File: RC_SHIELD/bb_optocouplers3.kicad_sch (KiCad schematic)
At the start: 15 parts, among them J1 Conn_01x04, U1 SFH6345, U2 SFH6345

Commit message: added secondary MCU to schematic and made it more consistent
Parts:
- removed J1 (x3): Conn_01x04, Connector_RJ:RJ9_Evercom_5301-440xxx_Horizontal, symbol Connector_Generic:Conn_01x04
- added R1 (x3), R2 (x3): 1K2, symbol Device:R
- added U1 (x3), U2 (x3): SFH6345, SFH6345:DIP762W50P254L977H451Q8, symbol SFH6345:SFH6345
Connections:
- net +3V3: now also U1.8, U1.8, U1.8, U2.8, U2.8, U2.8
- net GND: now also U2.5, U2.5, U2.5
- net GNDPWR: now also R1.2, R1.2, R1.2, R2.2, R2.2, R2.2
- net PHI_LIM_L_24: now reaches U2.2
- net PHI_LIM_R_24: now reaches U1.2
- net Z_LIM_TOP_24: now reaches U1.2
- net Z_LIM_BOT_24: now reaches U2.2
- net R_LIM_IN_24: now reaches U1.2
- net R_LIM_OUT_24: now reaches U2.2
- new net: R1.1, U1.3 (x3)
- new net: R2.1, U2.3 (x3)
- new net ALF_LIM_L: U2.6
- new net ALF_LIM_L_24: U2.2
- new net ALF_LIM_R: U1.6
- new net ALF_LIM_R_24: U1.2
- new net BET_LIM_DOWN: U2.6
- new net BET_LIM_DOWN_24: U2.2
- new net BET_LIM_UP: U1.6
- new net BET_LIM_UP_24: U1.2
- new net TH_LIM_CCW: U1.6
- new net TH_LIM_CCW_24: U1.2
- new net TH_LIM_CLW: U2.6
- new net TH_LIM_CLW_24: U2.2
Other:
- note removed: "PHI LimSwitch"
- note removed: "R LimSwitch"
- note removed: "Z LimSwitch"
- company: (none) -> LEGO Kör (legokor.hu)
- title: LIMIT SWITCHES -> Karcsi (INDACT Robot Arm) - limit switch optocouplers
- moved on the sheet: R1, R2, U1, U2

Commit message: footprints assigned
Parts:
- R1, R2: footprint (none) -> Resistor_SMD:R_0805_2012Metric_Pad1.20x1.40mm_HandSolder
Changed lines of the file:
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@@
       (effects (font (size 1.27 1.27)) (justify left))
     )
-    (property "Footprint" "" (at 211.582 45.085 90)
+    (property "Footprint" "Resistor_SMD:R_0805_2012Metric_Pad1.20x1.40mm_HandSolder" (at 211.582 45.085 90)
       (effects (font (size 1.27 1.27)) hide)
     )
@@
       (effects (font (size 1.27 1.27)) (justify left))
     )
-    (property "Footprint" "" (at 212.217 173.355 90)
+    (property "Footprint" "Resistor_SMD:R_0805_2012Metric_Pad1.20x1.40mm_HandSolder" (at 212.217 173.355 90)
       (effects (font (size 1.27 1.27)) hide)
     )
@@
       (effects (font (size 1.27 1.27)) (justify left))
     )
-    (property "Footprint" "" (at 111.887 86.995 90)
+    (property "Footprint" "Resistor_SMD:R_0805_2012Metric_Pad1.20x1.40mm_HandSolder" (at 111.887 86.995 90)
       (effects (font (size 1.27 1.27)) hide)
     )
@@
       (effects (font (size 1.27 1.27)) (justify left))
     )
-    (property "Footprint" "" (at 35.052 45.085 90)
+    (property "Footprint" "Resistor_SMD:R_0805_2012Metric_Pad1.20x1.40mm_HandSolder" (at 35.052 45.085 90)
       (effects (font (size 1.27 1.27)) hide)
     )
@@
       (effects (font (size 1.27 1.27)) (justify left))
     )
-    (property "Footprint" "" (at 35.052 86.995 90)
+    (property "Footprint" "Resistor_SMD:R_0805_2012Metric_Pad1.20x1.40mm_HandSolder" (at 35.052 86.995 90)
       (effects (font (size 1.27 1.27)) hide)
     )
@@
       (effects (font (size 1.27 1.27)) (justify left))
     )
-    (property "Footprint" "" (at 111.887 131.445 90)
+    (property "Footprint" "Resistor_SMD:R_0805_2012Metric_Pad1.20x1.40mm_HandSolder" (at 111.887 131.445 90)
       (effects (font (size 1.27 1.27)) hide)
     )
@@
       (effects (font (size 1.27 1.27)) (justify left))
     )
-    (property "Footprint" "" (at 35.052 173.355 90)
+    (property "Footprint" "Resistor_SMD:R_0805_2012Metric_Pad1.20x1.40mm_HandSolder" (at 35.052 173.355 90)
       (effects (font (size 1.27 1.27)) hide)
     )
@@
       (effects (font (size 1.27 1.27)) (justify left))
     )
-    (property "Footprint" "" (at 212.217 131.445 90)
+    (property "Footprint" "Resistor_SMD:R_0805_2012Metric_Pad1.20x1.40mm_HandSolder" (at 212.217 131.445 90)
       (effects (font (size 1.27 1.27)) hide)
     )
@@
       (effects (font (size 1.27 1.27)) (justify left))
     )
-    (property "Footprint" "" (at 111.887 173.355 90)
+    (property "Footprint" "Resistor_SMD:R_0805_2012Metric_Pad1.20x1.40mm_HandSolder" (at 111.887 173.355 90)
       (effects (font (size 1.27 1.27)) hide)
     )
@@
       (effects (font (size 1.27 1.27)) (justify left))
     )
-    (property "Footprint" "" (at 111.887 45.085 90)
+    (property "Footprint" "Resistor_SMD:R_0805_2012Metric_Pad1.20x1.40mm_HandSolder" (at 111.887 45.085 90)
       (effects (font (size 1.27 1.27)) hide)
     )
@@
       (effects (font (size 1.27 1.27)) (justify left))
     )
-    (property "Footprint" "" (at 35.052 131.445 90)
+    (property "Footprint" "Resistor_SMD:R_0805_2012Metric_Pad1.20x1.40mm_HandSolder" (at 35.052 131.445 90)
       (effects (font (size 1.27 1.27)) hide)
     )
@@
       (effects (font (size 1.27 1.27)) (justify left))
     )
-    (property "Footprint" "" (at 211.582 86.995 90)
-      (effects (font (size 1.27 1.27)) hide)
-    )
+    (property "Footprint" "Resistor_SMD:R_0805_2012Metric_Pad1.20x1.40mm_HandSolder" (at 211.582 86.995 90)
+      (effects (font (size 1.27 1.27)) hide)
+    )

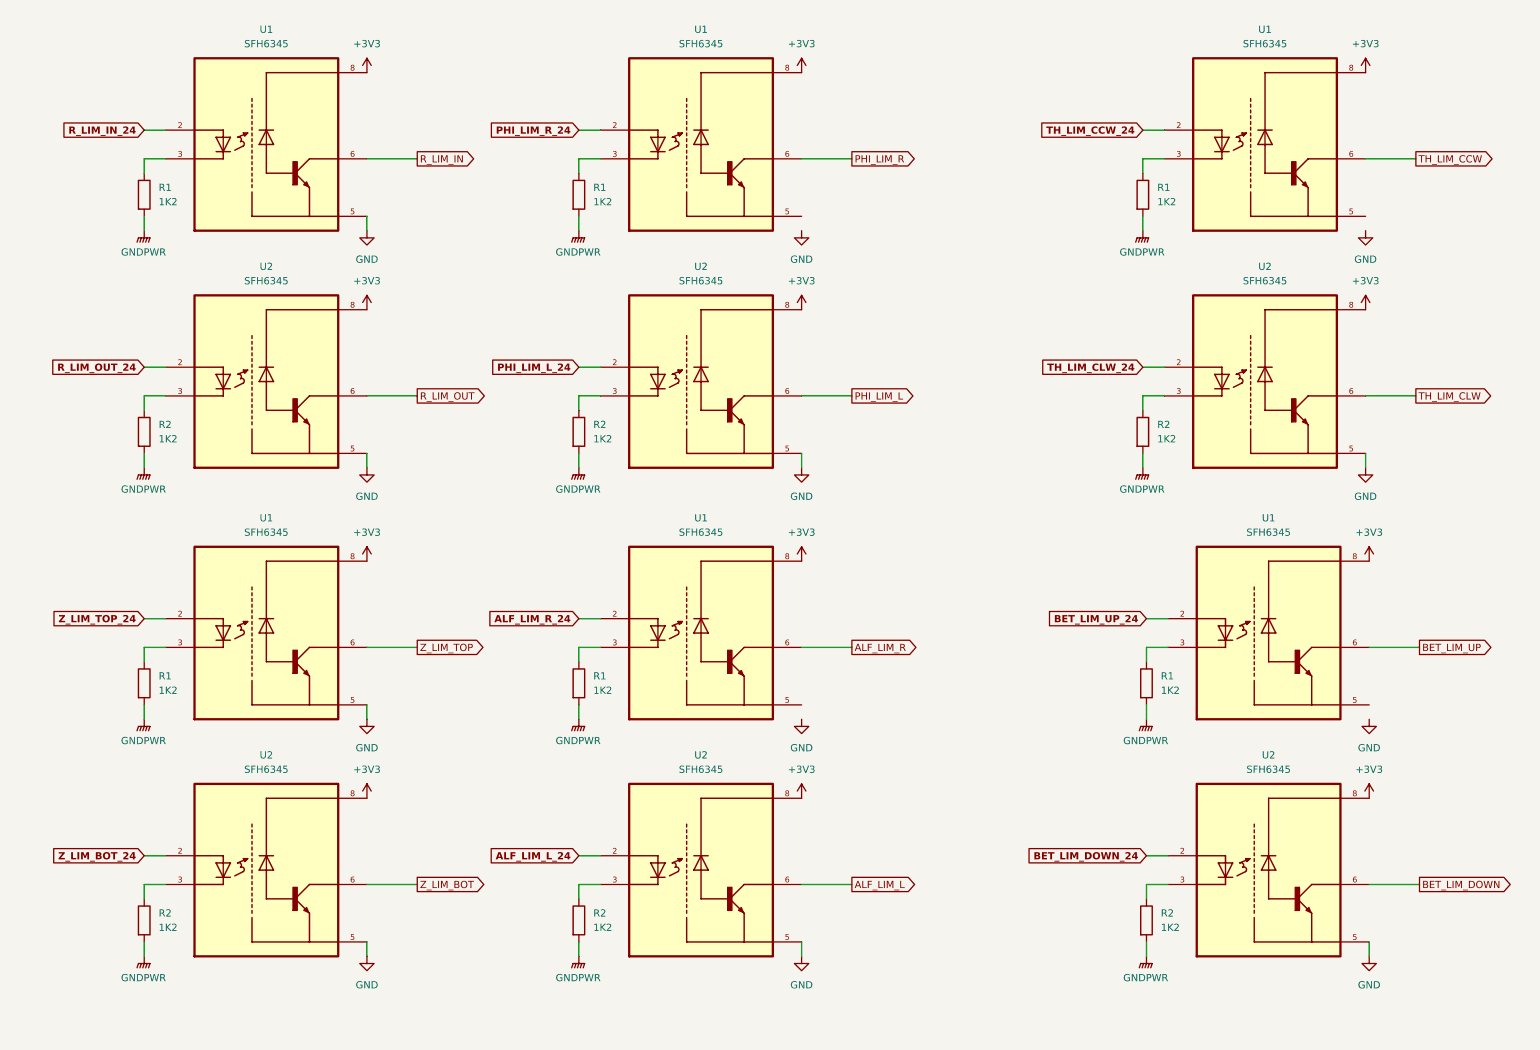
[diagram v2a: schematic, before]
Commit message: Fixed typos and names in schematic, changed optocoupler resistors; added .gitgnore file
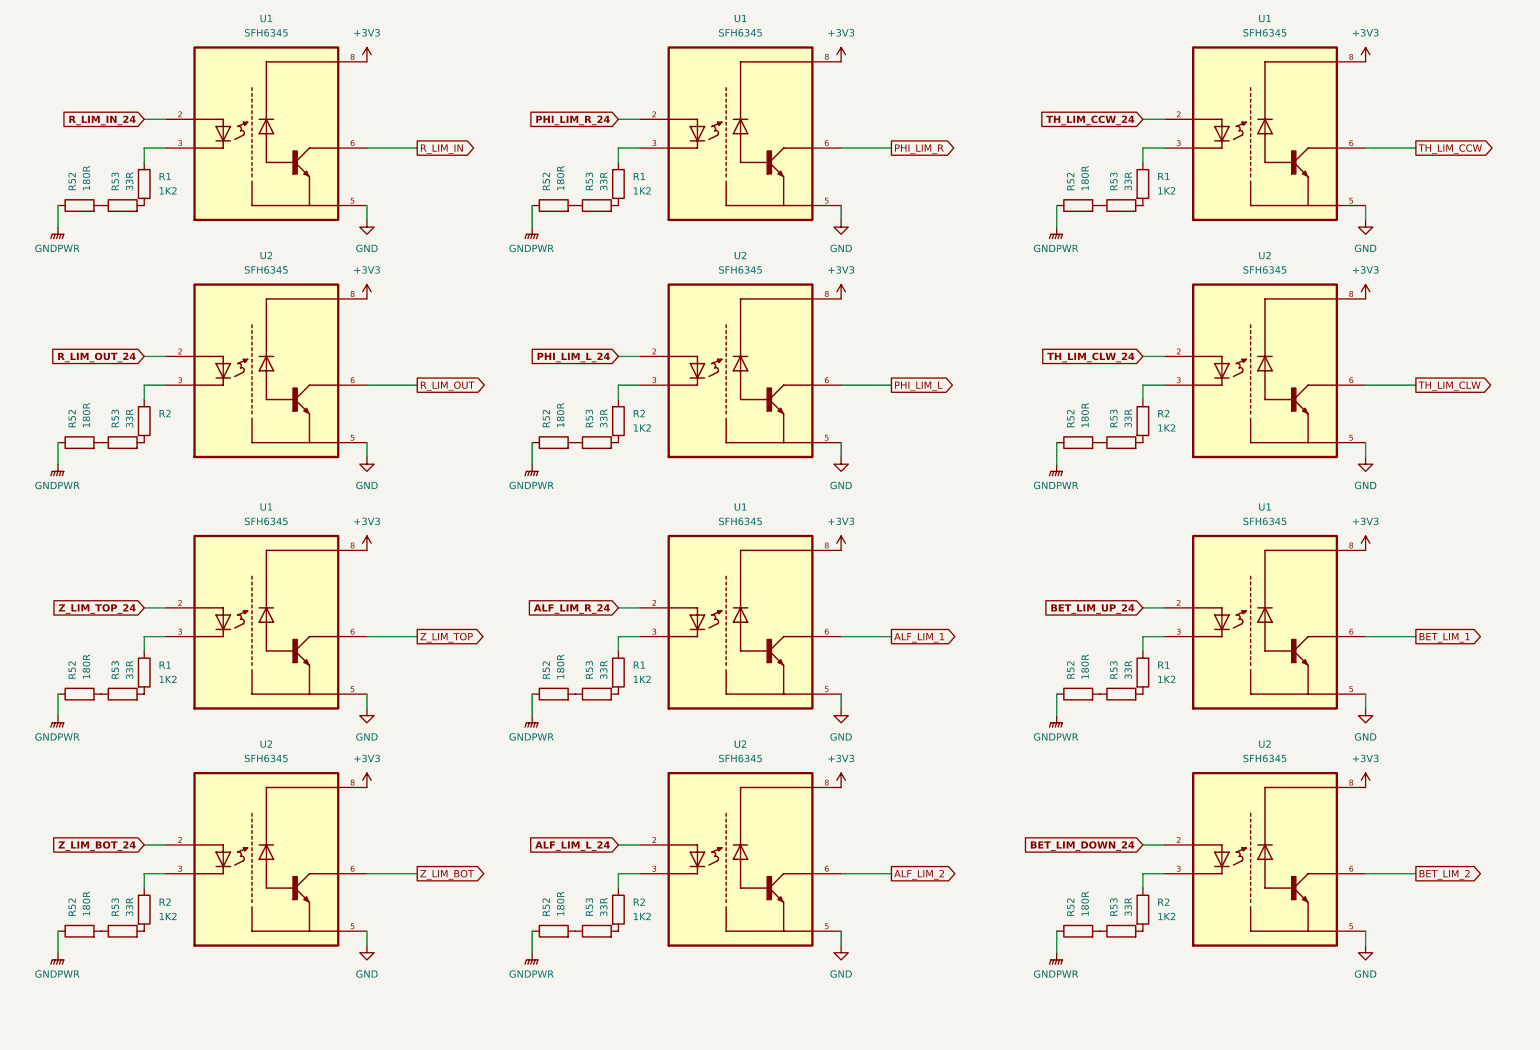
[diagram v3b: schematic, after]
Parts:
- added R52 (x12): 180R, Resistor_SMD:R_0805_2012Metric_Pad1.20x1.40mm_HandSolder, symbol Device:R
- added R53 (x12): 33R, Resistor_SMD:R_0805_2012Metric_Pad1.20x1.40mm_HandSolder, symbol Device:R
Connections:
- net GND: now also U1.5, U1.5, U1.5, U1.5
- net GNDPWR: now also R52.1, R52.1, R52.1, R52.1, R52.1, R52.1, R52.1, R52.1, R52.1, R52.1, R52.1, R52.1; no longer R1.2, R1.2, R1.2, R1.2, R1.2, R1.2, R2.2, R2.2, R2.2, R2.2, R2.2, R2.2
- net ALF_LIM_L renamed ALF_LIM_2
- net ALF_LIM_R renamed ALF_LIM_1
- net BET_LIM_DOWN renamed BET_LIM_2
- net BET_LIM_UP renamed BET_LIM_1
- new net: R52.2, R53.1 (x12)
- new net: R2.2, R53.2 (x6)
- new net: R1.2, R53.2 (x6)
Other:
- moved on the sheet: R1, R2, U1, U2

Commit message: [SCH] reorganized optocouplers and tidied up page 2
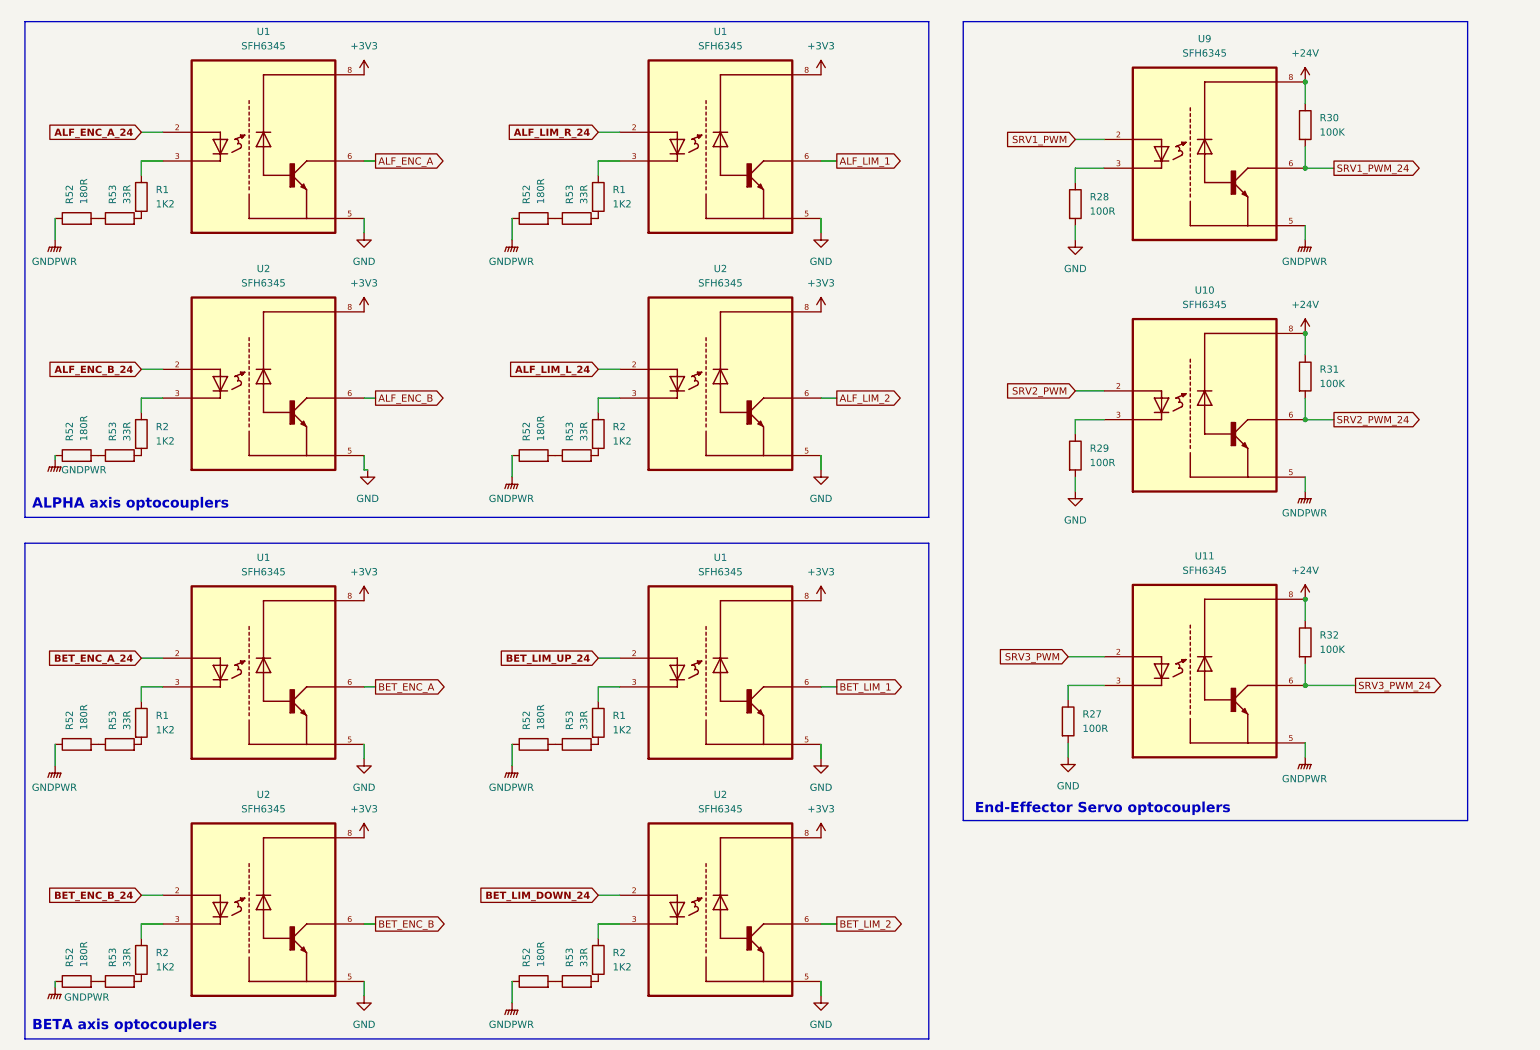
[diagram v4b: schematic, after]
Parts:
- removed R1 (x4), R2 (x4): 1K2, Resistor_SMD:R_0805_2012Metric_Pad1.20x1.40mm_HandSolder, symbol Device:R
- removed R52 (x8): 180R, Resistor_SMD:R_0805_2012Metric_Pad1.20x1.40mm_HandSolder, symbol Device:R
- removed R53 (x8): 33R, Resistor_SMD:R_0805_2012Metric_Pad1.20x1.40mm_HandSolder, symbol Device:R
- removed U1 (x4), U2 (x4): SFH6345, SFH6345:DIP762W50P254L977H451Q8, symbol SFH6345:SFH6345
- added R1 (x2), R2 (x2): 1K2, Resistor_SMD:R_0805_2012Metric_Pad1.20x1.40mm_HandSolder, symbol Device:R
- added R27, R28, R29: 100R, Resistor_SMD:R_0805_2012Metric_Pad1.20x1.40mm_HandSolder, symbol Device:R
- added R30, R31, R32: 100K, Resistor_SMD:R_0805_2012Metric_Pad1.20x1.40mm_HandSolder, symbol Device:R
- added R52 (x4): 180R, Resistor_SMD:R_0805_2012Metric_Pad1.20x1.40mm_HandSolder, symbol Device:R
- added R53 (x4): 33R, Resistor_SMD:R_0805_2012Metric_Pad1.20x1.40mm_HandSolder, symbol Device:R
- added U1 (x2), U10, U11, U2 (x2), U9: SFH6345, SFH6345:DIP762W50P254L977H451Q8, symbol SFH6345:SFH6345
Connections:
- net +3V3: now also U1.8, U1.8, U2.8, U2.8
- net GND: now also R27.2, R28.2, R29.2, U1.5, U1.5, U2.5, U2.5
- net GNDPWR: now also R52.1, R52.1, R52.1, R52.1, U10.5, U11.5, U9.5
- new net: R52.2, R53.1 (x4)
- new net: R2.2, R53.2 (x2)
- new net: R2.1, U2.3 (x2)
- new net: R1.1, U1.3 (x2)
- new net: R1.2, R53.2 (x2)
- new net: R29.1, U10.3
- new net: R27.1, U11.3
- new net: R28.1, U9.3
- new net +24V: R30.1, R31.1, R32.1, U10.8, U11.8, U9.8
- new net ALF_ENC_A: U1.6
- new net ALF_ENC_A_24: U1.2
- new net ALF_ENC_B: U2.6
- new net ALF_ENC_B_24: U2.2
- new net BET_ENC_A: U1.6
- new net BET_ENC_A_24: U1.2
- new net BET_ENC_B: U2.6
- new net BET_ENC_B_24: U2.2
- new net SRV1_PWM: U9.2
- new net SRV1_PWM_24: R30.2, U9.6
- new net SRV2_PWM: U10.2
- new net SRV2_PWM_24: R31.2, U10.6
- new net SRV3_PWM: U11.2
- new net SRV3_PWM_24: R32.2, U11.6
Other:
- note added: "ALPHA axis optocouplers"
- note added: "BETA axis optocouplers"
- note added: "End-Effector Servo optocouplers"
- moved on the sheet: R1, R2, R52, R53, U1, U2

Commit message: [SCH] added "exclude from BOM" signs
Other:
- title: Karcsi (INDACT Robot Arm) - limit switch optocouplers -> Karcsi (INDACT Robot Arm) - Wrist & EE optocouplers
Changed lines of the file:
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@@
   (paper "A4")
   (title_block
-    (title "Karcsi (INDACT Robot Arm) - limit switch optocouplers")
+    (title "Karcsi (INDACT Robot Arm) - Wrist & EE optocouplers")
     (date "2023-10-07")
     (rev "1.1")
